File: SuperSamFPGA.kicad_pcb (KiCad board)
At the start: 6 copper layers, 63.7 x 82.3 mm, 103 parts, among them J1 DataBus, J2 Video, J3 AddressBus, J4 ControlOut, J5 ControlIn, J6 JTAG, J7 BusService, SW1 Tactile, U1 74LVC573, U10 TXS0108EPW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

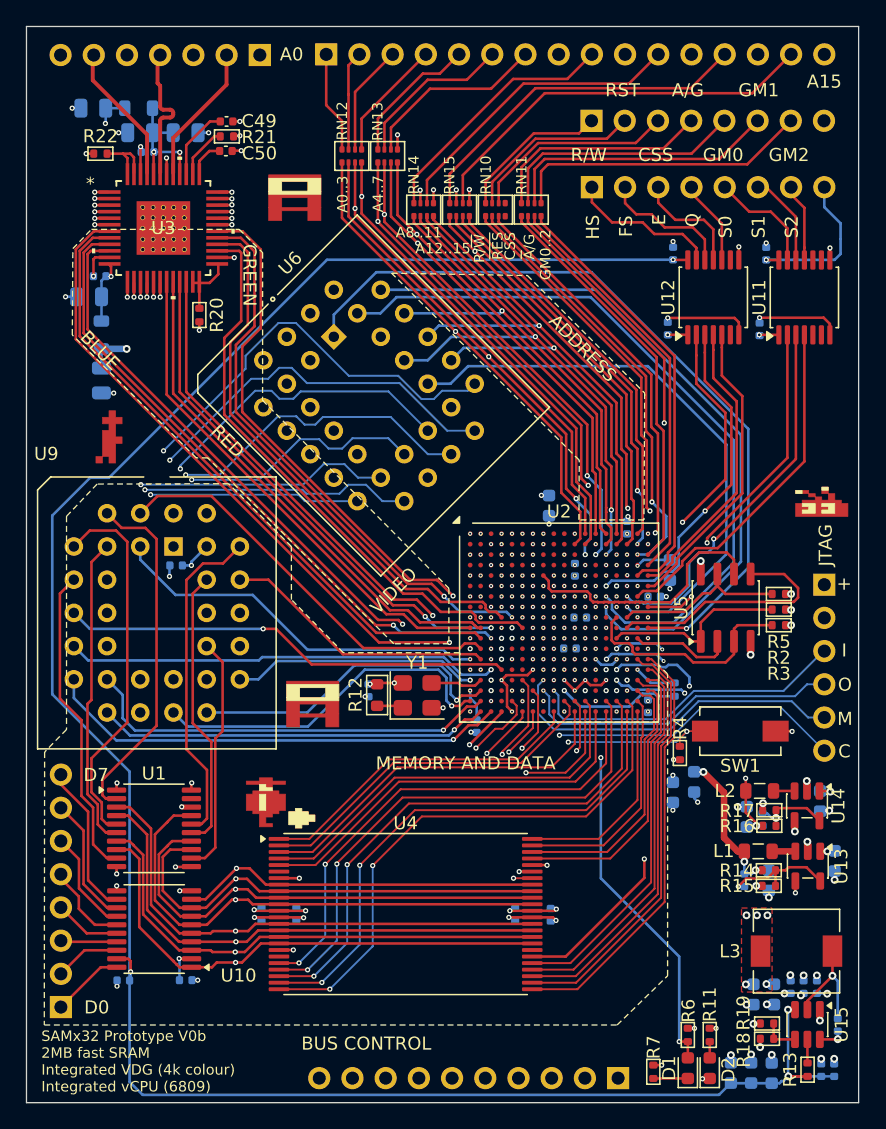
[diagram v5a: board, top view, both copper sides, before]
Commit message: complete primary routing
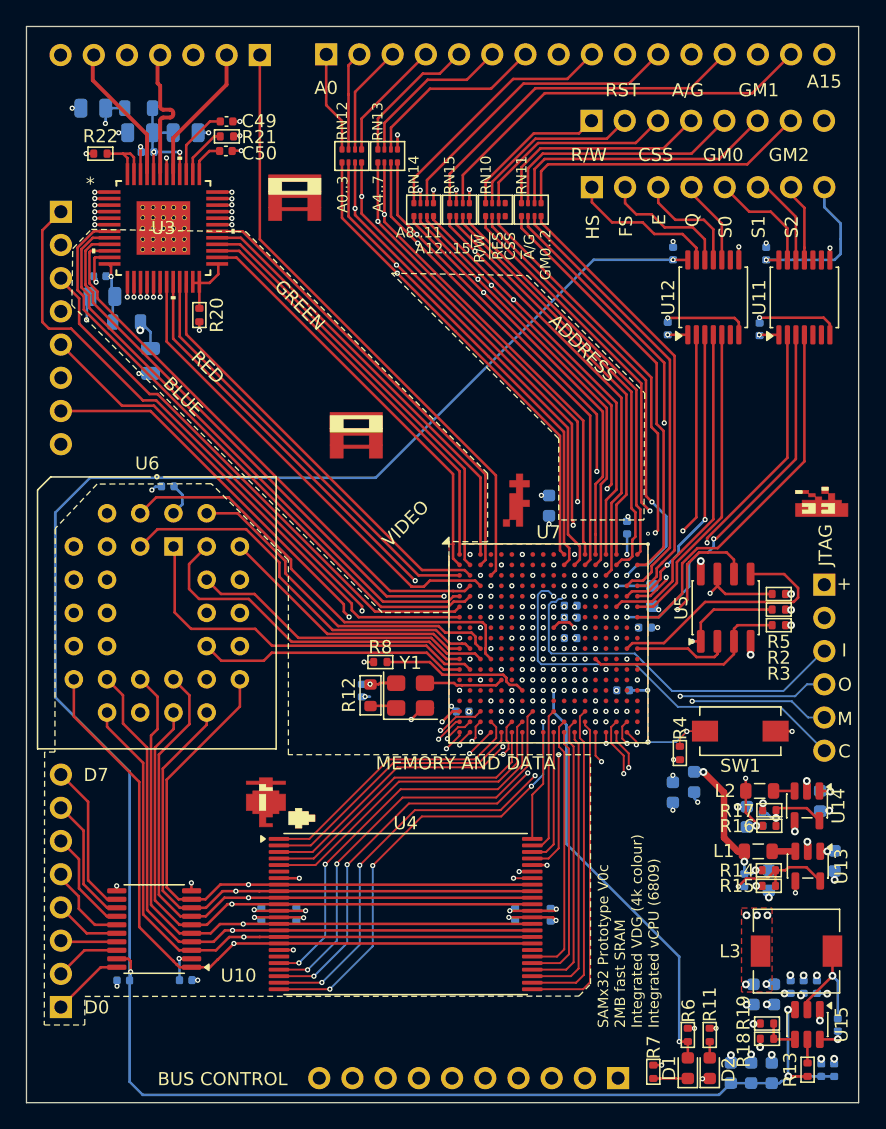
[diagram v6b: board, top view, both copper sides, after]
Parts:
- removed R1: 4.7K, PCM_Resistor_SMD_AKL:R_0402_1005Metric
- removed U1: 74LVC573, Package_SO:TSSOP-20_4.4x6.5mm_P0.65mm
- removed U2: XC7A15T-CSG325, Package_BGA:BGA-324_15x15mm_Layout18x18_P0.8mm
- removed U9: AT28BV64B-20JU, Package_LCC:PLCC-32_THT-Socket
- added J8: AudioOut, Connector_PinHeader_2.54mm:PinHeader_1x08_P2.54mm_Vertical, B.Cu at (120.3, 67.0)
- added R8: 4.7K, PCM_Resistor_SMD_AKL:R_0402_1005Metric, F.Cu at (144.8, 101.5)
- added U7: XC7A35T-CSG324, Package_BGA:BGA-324_15x15mm_Layout18x18_P0.8mm, F.Cu at (157.6, 100.0)
- moved U6 20.2 mm to (128.9, 92.6), turned to 0 degrees
- moved C46 6.08 mm to (128.5, 88.0)
- moved C24 4.04 mm to (127.2, 78.4)
- moved C8 2.76 mm to (159.3, 97.2), turned to 180 degrees
- moved C2 2.47 mm to (165.0, 98.8)
- moved C1 2.40 mm to (165.6, 96.4)
- moved C3 2.26 mm to (163.3, 103.6), turned to 0 degrees
- moved L4 2.17 mm to (125.3, 75.5), turned to 180 degrees
- moved C4 1.55 mm to (151.1, 105.3), turned to 180 degrees
- moved C28 1.02 mm to (123.5, 73.5)
- moved C11 0.79 mm to (159.3, 99.6), turned to 0 degrees
- moved C10 0.73 mm to (159.3, 98.1), turned to 0 degrees
- moved R12 0.51 mm to (144.0, 104.0)
- moved Y1 0.51 mm to (147.1, 104.0)
- moved C25 0.51 mm to (143.3, 103.7)
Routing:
- net /RD6: track 166.2 -> 71.8 mm, vias 3 -> 2
- net /RD4: track 165.5 -> 72.2 mm, vias 3 -> 2
- net /RD7: track 163.5 -> 73.9 mm, vias 3 -> 2
- net /RD5: track 160.9 -> 75.8 mm, vias 3 -> 2
- net /RD3: track 158.3 -> 79.0 mm, vias 3 -> 2
- net /RD2: track 152.3 -> 79.8 mm, vias 3 -> 2
- net /RD1: track 153.1 -> 81.9 mm, vias 3 -> 2
- net /RD0: track 147.4 -> 85.9 mm, vias 3 -> 2
- net /BCLK: track 0.00 -> 52.1 mm, vias 0 -> 2
- net /WS: track 0.00 -> 42.4 mm
- net /MCLK: track 0.00 -> 39.8 mm, vias 0 -> 2
- net /SD: track 0.00 -> 39.4 mm
- net /CD0: track 35.6 -> 0.00 mm, vias 1 -> 0
- net /RZ14: track 55.3 -> 20.0 mm, vias 1 -> 0
- net /CR2: track 34.5 -> 0.00 mm, vias 1 -> 0
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- added copper zone on F.Cu, net GND
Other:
- board text added: "SAMx32 Prototype V0c 2MB fast SRAM Integrated VDG (4k colour) Integrated vCPU (6809)"
- board text removed: "CHAR DATA"
- board text removed: "SAMx32 Prototype V0b 2MB fast SRAM Integrated VDG (4k colour) Integrated vCPU (6809)"
